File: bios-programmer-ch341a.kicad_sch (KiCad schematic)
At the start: 50 parts, among them J1 USB_B_Micro, J2 SPI Debug, J3 I²C Debug, J4 -Banana-, J5 +Banana+, J6 ZIF16, J7 Conn_02x05_Odd_Even, J8 Conn_02x05_Odd_Even, J9 SENSE, Q1 SSM3J328R, Q2 SSM3J328R, Q3 SSM3J328R, Q4 SSM3J328R, SW1 RESET, U1 CH341A, U2 ISO6741, U3 ADuM1252, U4 TL432DBZ, Y1 12MHz

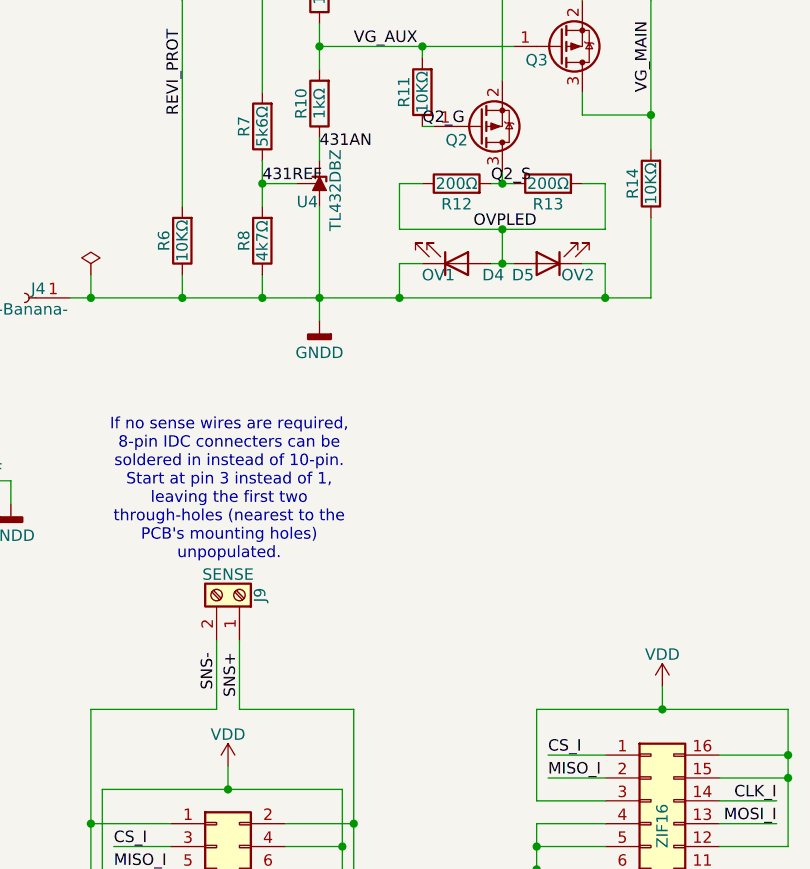
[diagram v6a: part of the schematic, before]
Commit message: PCB: additional LED resistor
Previously having 2 resistors in parallel, leading to 2 parallel LEDs could
potentially lead to an issue in case any of the LEDs fails or burns out. The
other remaining LED would then have to bear all of the current and surely burn
out as well.

Note that the LEDs are already potentially overdriven, depening on the input
voltage. That said, no more than 8V is supported for the power protection path
anyway.
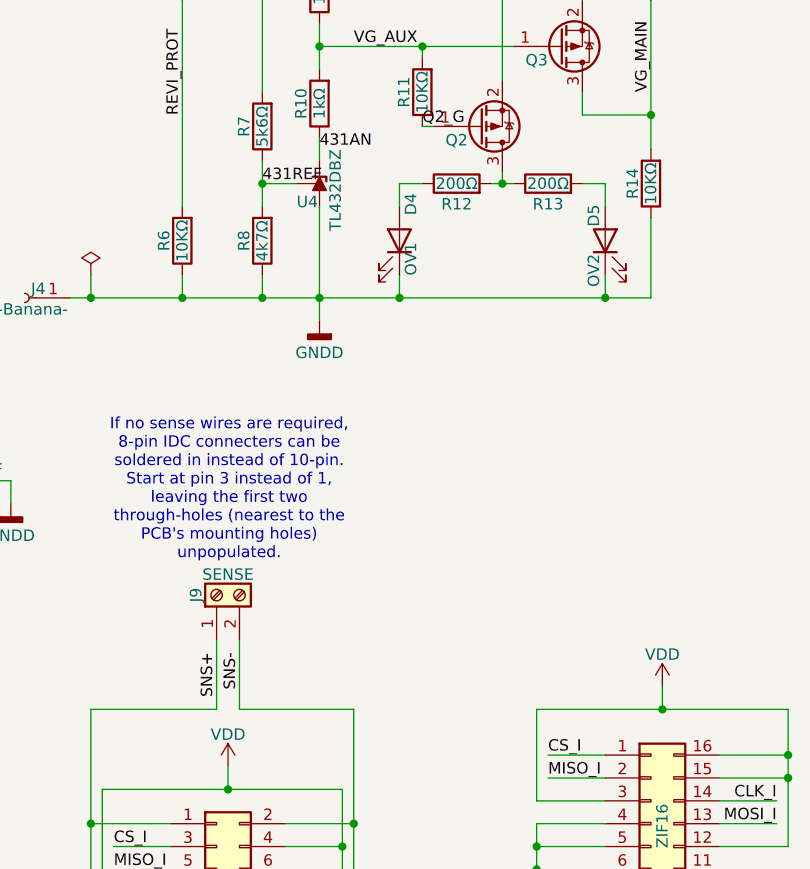
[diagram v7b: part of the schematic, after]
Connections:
- net SNS+: now also J7.1 (Pin_1), J8.1 (Pin_1); no longer J7.2 (Pin_2), J8.2 (Pin_2)
- net SNS-: now also J7.2 (Pin_2), J8.2 (Pin_2); no longer J7.1 (Pin_1), J8.1 (Pin_1)
- net OVPLED: no longer names the net of D5.2 (A), R13.2
- net OVPLED: no longer D4.2 (A), R12.1
- net Q2_S: no longer names the net of Q2.3 (D), R12.2, R13.1
- new net: D4.2 (A), R12.1
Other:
- moved on the sheet: D4, D5, J9
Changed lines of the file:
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@@
 	)
 	(junction
-		(at 236.22 54.61)
-		(diameter 0)
-		(color 0 0 0 0)
-	)
-	(junction
 		(at 236.22 49.53)
 		(diameter 0)
@@
 	)
 	(junction
-		(at 236.22 58.42)
-		(diameter 0)
-		(color 0 0 0 0)
-	)
-	(junction
 		(at 80.01 71.12)
 		(diameter 0)
@@
 	(wire
 		(pts
+			(xy 224.79 49.53) (xy 224.79 52.07)
+		)
+		(stroke
+			(width 0)
+			(type default)
+		)
+	)
+	(wire
+		(pts
 			(xy 190.5 62.23) (xy 200.66 62.23)
 		)
@@
 	(wire
 		(pts
-			(xy 247.65 49.53) (xy 247.65 54.61)
-		)
-		(stroke
-			(width 0)
-			(type default)
-		)
-	)
-	(wire
-		(pts
 			(xy 129.54 50.8) (xy 129.54 48.26)
 		)
@@
 	(wire
 		(pts
-			(xy 236.22 58.42) (xy 237.49 58.42)
-		)
-		(stroke
-			(width 0)
-			(type default)
-		)
-	)
-	(wire
-		(pts
 			(xy 146.05 133.35) (xy 151.13 133.35)
 		)
@@
 	(wire
 		(pts
-			(xy 224.79 58.42) (xy 224.79 62.23)
-		)
-		(stroke
-			(width 0)
-			(type default)
-		)
-	)
-	(wire
-		(pts
 			(xy 146.05 125.73) (xy 146.05 133.35)
 		)
@@
 	(wire
 		(pts
-			(xy 234.95 58.42) (xy 236.22 58.42)
-		)
-		(stroke
-			(width 0)
-			(type default)
-		)
-	)
-	(wire
-		(pts
 			(xy 171.45 133.35) (xy 176.53 133.35)
 		)
@@
 	(wire
 		(pts
-			(xy 224.79 58.42) (xy 227.33 58.42)
-		)
-		(stroke
-			(width 0)
-			(type default)
-		)
-	)
-	(wire
-		(pts
 			(xy 69.85 101.6) (xy 36.83 101.6)
 		)
@@
 	(wire
 		(pts
-			(xy 224.79 49.53) (xy 224.79 54.61)
-		)
-		(stroke
-			(width 0)
-			(type default)
-		)
-	)
-	(wire
-		(pts
 			(xy 55.88 111.76) (xy 59.69 111.76)
 		)
@@
 	(wire
 		(pts
-			(xy 66.04 129.54) (xy 66.04 143.51)
+			(xy 247.65 59.69) (xy 247.65 62.23)
 		)
 		(stroke
@@
 	(wire
 		(pts
-			(xy 53.34 73.66) (xy 53.34 71.12)
+			(xy 66.04 129.54) (xy 66.04 143.51)
 		)
 		(stroke
@@
 	(wire
 		(pts
-			(xy 127 82.55) (xy 127 87.63)
+			(xy 53.34 73.66) (xy 53.34 71.12)
 		)
 		(stroke
@@
 	(wire
 		(pts
-			(xy 80.01 71.12) (xy 85.09 71.12)
+			(xy 127 82.55) (xy 127 87.63)
 		)
 		(stroke
@@
 	(wire
 		(pts
-			(xy 247.65 58.42) (xy 247.65 62.23)
+			(xy 80.01 71.12) (xy 85.09 71.12)
 		)
 		(stroke
@@
 	(wire
 		(pts
-			(xy 247.65 54.61) (xy 236.22 54.61)
-		)
-		(stroke
-			(width 0)
-			(type default)
-		)
-	)
-	(wire
-		(pts
 			(xy 212.09 144.78) (xy 219.71 144.78)
 		)
@@
 	(wire
 		(pts
-			(xy 224.79 54.61) (xy 236.22 54.61)
-		)
-		(stroke
-			(width 0)
-			(type default)
-		)
-	)
-	(wire
-		(pts
 			(xy 240.03 130.81) (xy 240.03 135.89)
 		)
@@
 	(wire
 		(pts
-			(xy 236.22 54.61) (xy 236.22 58.42)
+			(xy 127 45.72) (xy 127 60.96)
 		)
 		(stroke
@@
 	(wire
 		(pts
-			(xy 127 45.72) (xy 127 60.96)
+			(xy 190.5 120.65) (xy 199.39 120.65)
 		)
 		(stroke
@@
 	(wire
 		(pts
-			(xy 190.5 120.65) (xy 199.39 120.65)
+			(xy 247.65 49.53) (xy 247.65 52.07)
 		)
 		(stroke
@@
 	(wire
 		(pts
+			(xy 224.79 59.69) (xy 224.79 62.23)
+		)
+		(stroke
+			(width 0)
+			(type default)
+		)
+	)
+	(wire
+		(pts
 			(xy 171.45 130.81) (xy 173.99 130.81)
 		)
@@
 		)
 	)
-	(wire
-		(pts
-			(xy 245.11 58.42) (xy 247.65 58.42)
-		)
-		(stroke
-			(width 0)
-			(type default)
-		)
-	)
 	(label "CLK_I"
 		(at 266.7 118.11 180)
@@
 	)
 	(label "SNS-"
-		(at 204.47 101.6 270)
+		(at 207.01 101.6 270)
 		(effects
 			(font
@@
 		)
 	)
-	(label "Q2_S"
-		(at 234.95 49.53 0)
-		(effects
-			(font
-				(size 1.27 1.27)
-			)
-			(justify left bottom)
-		)
-	)
 	(label "SCL_I"
 		(at 266.7 128.27 180)
@@
 	)
 	(label "SNS+"
-		(at 207.01 101.6 270)
+		(at 204.47 101.6 270)
 		(effects
 			(font
@@
 		)
 	)
-	(label "OVPLED"
-		(at 240.03 54.61 180)
-		(effects
-			(font
-				(size 1.27 1.27)
-			)
-			(justify right bottom)
-		)
-	)
 	(label "SCL_I"
 		(at 218.44 152.4 180)
@@
 	(symbol
 		(lib_id "Device:LED")
-		(at 241.3 58.42 180)
+		(at 247.65 55.88 90)
 		(unit 1)
 		(body_style 1)
@@
 		(dnp no)
 		(property "Reference" "D5"
-			(at 238.506 59.69 0)
+			(at 246.38 53.086 0)
 			(show_name no)
 			(do_not_autoplace no)
@@
 		)
 		(property "Value" "OV2"
-			(at 244.602 59.69 0)
+			(at 246.38 59.182 0)
 			(show_name no)
 			(do_not_autoplace no)
@@
 		)
 		(property "Footprint" "LED_SMD:LED_0805_2012Metric_Pad1.15x1.40mm_HandSolder"
-			(at 241.3 58.42 0)
+			(at 247.65 55.88 0)
 			(hide yes)
 			(show_name no)
@@
 		)
 		(property "Datasheet" ""
-			(at 241.3 58.42 0)
+			(at 247.65 55.88 0)
 			(hide yes)
 			(show_name no)
@@
 		)
 		(property "Description" "Light emitting diode"
-			(at 241.3 58.42 0)
+			(at 247.65 55.88 0)
 			(hide yes)
 			(show_name no)
@@
 		)
 		(property "Sim.Pins" "1=K 2=A"
-			(at 241.3 58.42 0)
+			(at 247.65 55.88 0)
 			(hide yes)
 			(show_name no)
@@
 	(symbol
 		(lib_id "Device:LED")
-		(at 231.14 58.42 0)
+		(at 224.79 55.88 270)
 		(mirror x)
 		(unit 1)
@@
 		(dnp no)
 		(property "Reference" "D4"
-			(at 235.204 59.69 0)
+			(at 226.06 51.816 0)
 			(show_name no)
 			(do_not_autoplace no)
@@
 		)
 		(property "Value" "OV1"
-			(at 229.108 59.69 0)
+			(at 226.06 57.912 0)
 			(show_name no)
 			(do_not_autoplace no)
@@
 		)
 		(property "Footprint" "LED_SMD:LED_0805_2012Metric_Pad1.15x1.40mm_HandSolder"
-			(at 231.14 58.42 0)
+			(at 224.79 55.88 0)
 			(hide yes)
 			(show_name no)
@@
 		)
 		(property "Datasheet" ""
-			(at 231.14 58.42 0)
+			(at 224.79 55.88 0)
 			(hide yes)
 			(show_name no)
@@
 		)
 		(property "Description" "Light emitting diode"
-			(at 231.14 58.42 0)
+			(at 224.79 55.88 0)
 			(hide yes)
 			(show_name no)
@@
 		)
 		(property "Sim.Pins" "1=K 2=A"
-			(at 231.14 58.42 0)
+			(at 224.79 55.88 0)
 			(hide yes)
 			(show_name no)
@@
 	(symbol
 		(lib_id "Connector:Screw_Terminal_01x02")
-		(at 207.01 95.25 270)
-		(mirror x)
+		(at 204.47 95.25 90)
 		(unit 1)
 		(body_style 1)
@@
 		(dnp no)
 		(property "Reference" "J9"
-			(at 209.296 95.25 0)
+			(at 202.184 95.25 0)
 			(show_name no)
 			(do_not_autoplace no)
@@
 		)
 		(property "Footprint" "TerminalBlock_TE-Connectivity:TerminalBlock_TE_282834-2_1x02_P2.54mm_Horizontal"
-			(at 207.01 95.25 0)
+			(at 204.47 95.25 0)
 			(hide yes)
 			(show_name no)
@@
 		)
 		(property "Datasheet" ""
-			(at 207.01 95.25 0)
+			(at 204.47 95.25 0)
 			(hide yes)
 			(show_name no)
@@
 		)
 		(property "Description" "Generic screw terminal, single row, 01x02, script generated (kicad-library-utils/schlib/autogen/connector/)"
-			(at 207.01 95.25 0)
+			(at 204.47 95.25 0)
 			(hide yes)
 			(show_name no)

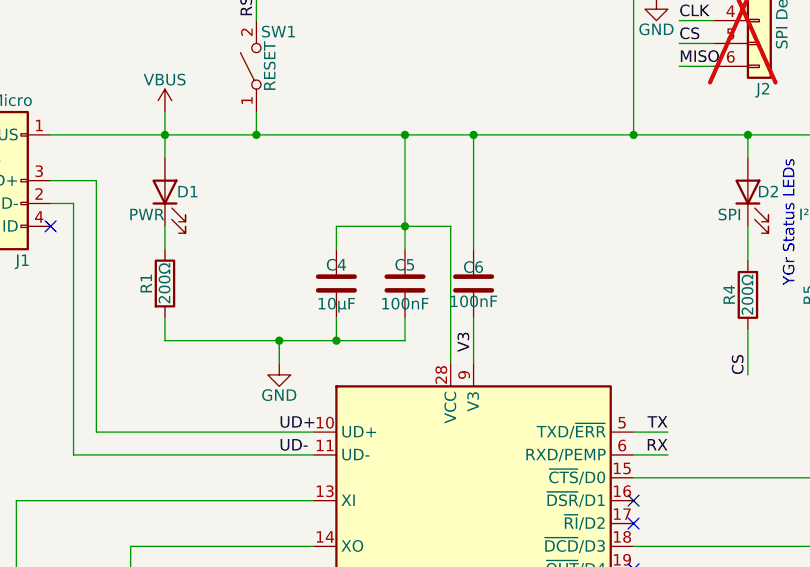
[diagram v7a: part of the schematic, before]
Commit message: SCH&PCB: set C5 to DNP, not in the datasheet
A 100nF capacitor is not in datasheet, but really the reason I removed it is
because it's hard to place without reducing the GND zone to a thin track.
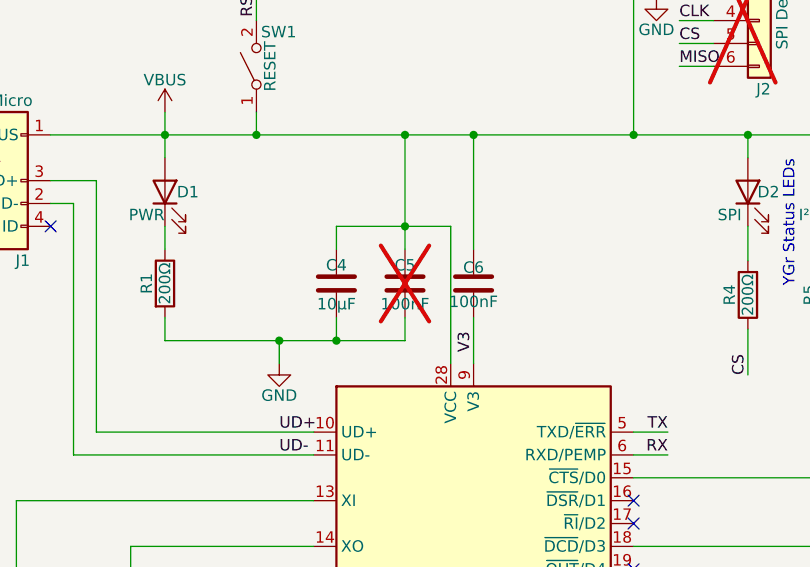
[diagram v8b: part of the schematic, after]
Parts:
- C5: now not fitted
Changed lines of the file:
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@@
 		(exclude_from_sim no)
 		(in_bom yes)
-		(on_board yes)
-		(in_pos_files yes)
-		(dnp no)
+		(on_board no)
+		(in_pos_files no)
+		(dnp yes)
 		(property "Reference" "C5"
 			(at 80.01 75.438 0)
